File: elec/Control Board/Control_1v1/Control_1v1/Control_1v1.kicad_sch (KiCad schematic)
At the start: 163 parts, among them J1 DB9_Female_MountingHoles, J10 Conn_02x12_Odd_Even, J11 Screw_Terminal_01x02, J14 Conn_01x10, J2 Conn_01x08, J25 Screw_Terminal_01x02, J26 Conn_01x10, J27 Conn_02x12_Odd_Even, J28 Screw_Terminal_01x02, J29 Conn_01x10, J3 Conn_01x08, J37 Conn_01x04, J4 Conn_01x08, J5 Conn_01x08, J6 Conn_01x08, J7 Conn_01x10, J8 Conn_02x18_Odd_Even, J9 Conn_01x10, Q601 BSS138

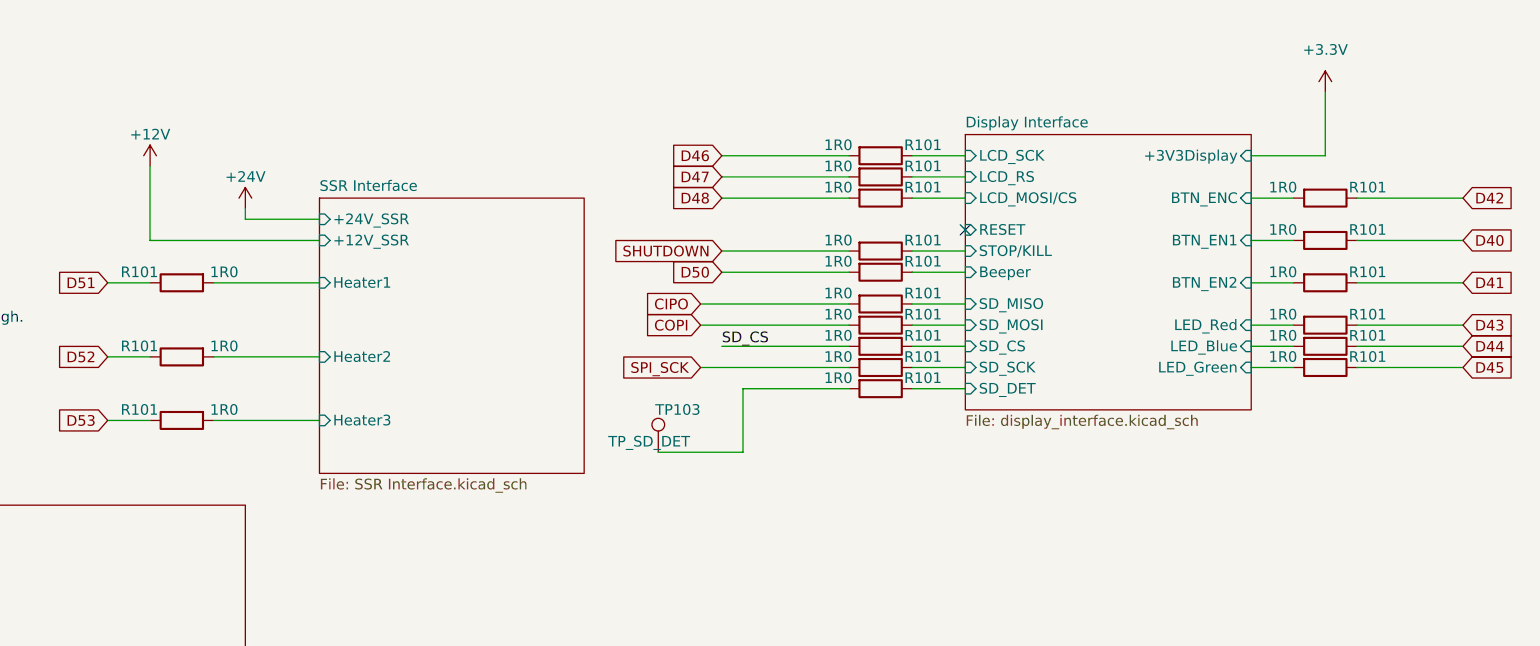
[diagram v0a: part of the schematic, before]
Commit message: Update schematic to reflect some reworks to V1.1 assemblies. 5V to Display. Display signal names. J35 pin8 to 10 short.
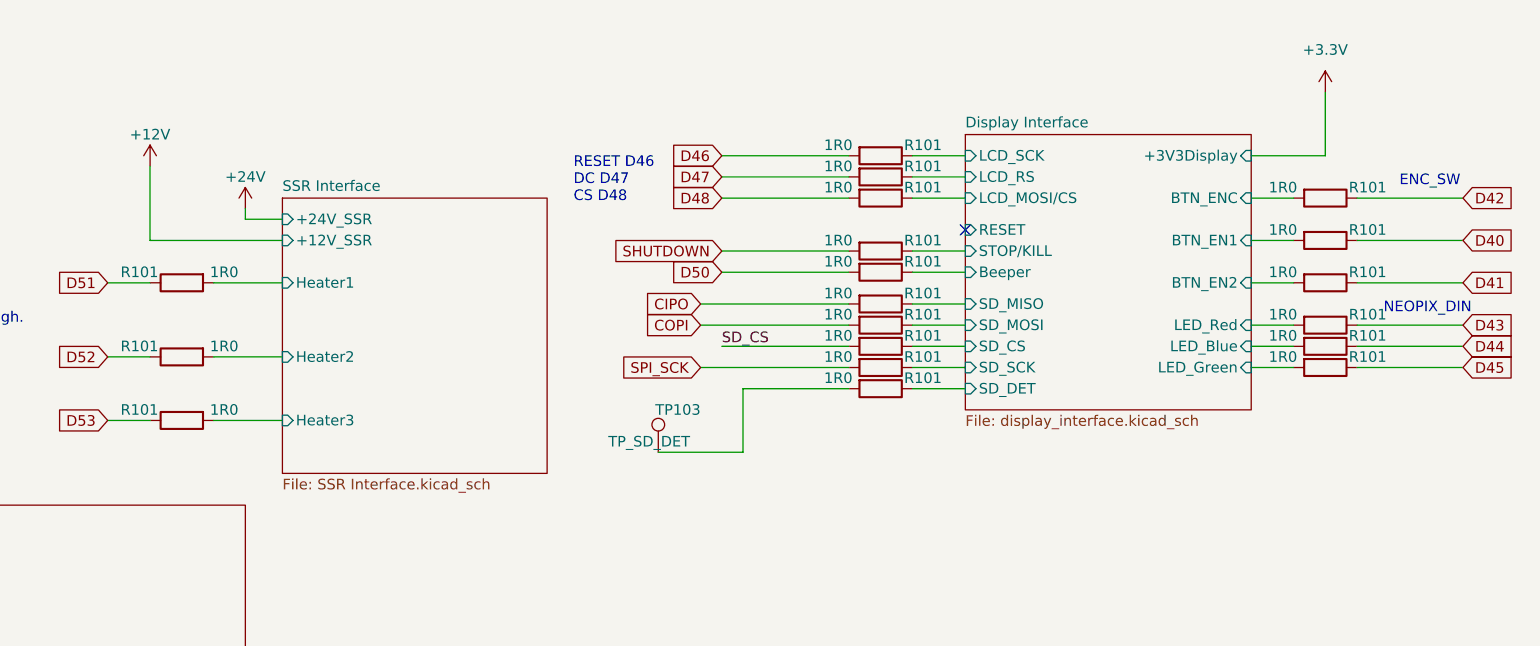
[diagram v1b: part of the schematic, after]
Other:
- note added: "ENC_SW"
- note added: "NEOPIX_DIN"
- note added: "RESET D46 DC D47 CS D48"
- title: Control Interconnect Board OEDCS -> Control Interconnect Board OEDCS With Reworks
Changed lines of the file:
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@@
   (paper "User" 533.4 330.2)
   (title_block
-    (title "Control Interconnect Board OEDCS")
-    (date "2023-10-10")
+    (title "Control Interconnect Board OEDCS With Reworks")
+    (date "2023-12-06")
     (rev "Rev 1.1")
     (company "Public Invention")
@@
     (stroke (width 0) (type default))
   )
-  (wire (pts (xy 377.19 248.92) (xy 368.3 248.92))
+  (wire (pts (xy 372.745 248.92) (xy 368.3 248.92))
     (stroke (width 0) (type default))
   )
@@
     (stroke (width 0) (type default))
   )
-  (wire (pts (xy 364.49 265.43) (xy 377.19 265.43))
+  (wire (pts (xy 364.49 265.43) (xy 372.745 265.43))
     (stroke (width 0) (type default))
   )
@@
     (stroke (width 0) (type default))
   )
-  (wire (pts (xy 364.49 256.54) (xy 377.19 256.54))
+  (wire (pts (xy 364.49 256.54) (xy 372.745 256.54))
     (stroke (width 0) (type default))
   )
@@
     (stroke (width 0) (type default))
   )
-  (wire (pts (xy 364.49 273.05) (xy 377.19 273.05))
+  (wire (pts (xy 364.49 273.05) (xy 372.745 273.05))
     (stroke (width 0) (type default))
   )
@@
     (stroke (width 0) (type default))
   )
-  (wire (pts (xy 377.19 251.46) (xy 356.87 251.46))
+  (wire (pts (xy 372.745 251.46) (xy 356.87 251.46))
     (stroke (width 0) (type default))
   )
@@
     (effects (font (size 1.27 1.27)) (justify left bottom))
   )
+  (text "ENC_SW" (at 506.73 245.11 0)
+    (effects (font (size 1.27 1.27)) (justify left bottom))
+  )
   (text "Blower Controller Signals\nFAN_POWER the Due output sets high to enable power to the blower.\nFAN1_FG is the Due input gets tachometer signal. Two low going edeges per revoluion.\nnFan1_PWM is negative aserted PWM to control blower speed."
     (at 302.26 189.23 0)
     (effects (font (size 1.27 1.27)) (justify left bottom))
   )
+  (text "NEOPIX_DIN" (at 504.825 260.35 0)
+    (effects (font (size 1.27 1.27)) (justify left bottom))
+  )
   (text "Logic Level i2c Connector" (at 35.56 287.02 0)
     (effects (font (size 1.27 1.27)) (justify left bottom))
@@
     (effects (font (size 1.27 1.27)) (justify left bottom))
   )
+  (text "RESET D46\nDC D47\nCS D48" (at 407.67 247.015 0)
+    (effects (font (size 1.27 1.27)) (justify left bottom))
+  )
   (text "One Wire Thermocouple amplifiter and Interface\nDATA is bidorectional on the Due GPIO"
     (at 92.71 154.94 0)
@@
     )
   )
-  (sheet (at 377.19 246.38) (size 31.75 33.02) (fields_autoplaced)
+  (sheet (at 372.745 246.38) (size 31.75 33.02) (fields_autoplaced)
     (stroke (width 0.1524) (type solid))
     (fill (color 0 0 0 0.0000))
-    (property "Sheetname" "SSR Interface" (at 377.19 245.6684 0)
+    (property "Sheetname" "SSR Interface" (at 372.745 245.6684 0)
       (effects (font (size 1.27 1.27)) (justify left bottom))
     )
-    (property "Sheetfile" "SSR Interface.kicad_sch" (at 377.19 279.9846 0)
+    (property "Sheetfile" "SSR Interface.kicad_sch" (at 372.745 279.9846 0)
       (effects (font (size 1.27 1.27)) (justify left top))
     )
-    (pin "+24V_SSR" input (at 377.19 248.92 180)
+    (pin "+24V_SSR" input (at 372.745 248.92 180)
       (effects (font (size 1.27 1.27)) (justify left))
     )
-    (pin "+12V_SSR" input (at 377.19 251.46 180)
+    (pin "+12V_SSR" input (at 372.745 251.46 180)
       (effects (font (size 1.27 1.27)) (justify left))
     )
-    (pin "Heater1" input (at 377.19 256.54 180)
+    (pin "Heater1" input (at 372.745 256.54 180)
       (effects (font (size 1.27 1.27)) (justify left))
     )
-    (pin "Heater2" input (at 377.19 265.43 180)
+    (pin "Heater2" input (at 372.745 265.43 180)
       (effects (font (size 1.27 1.27)) (justify left))
     )
-    (pin "Heater3" input (at 377.19 273.05 180)
+    (pin "Heater3" input (at 372.745 273.05 180)
       (effects (font (size 1.27 1.27)) (justify left))
     )

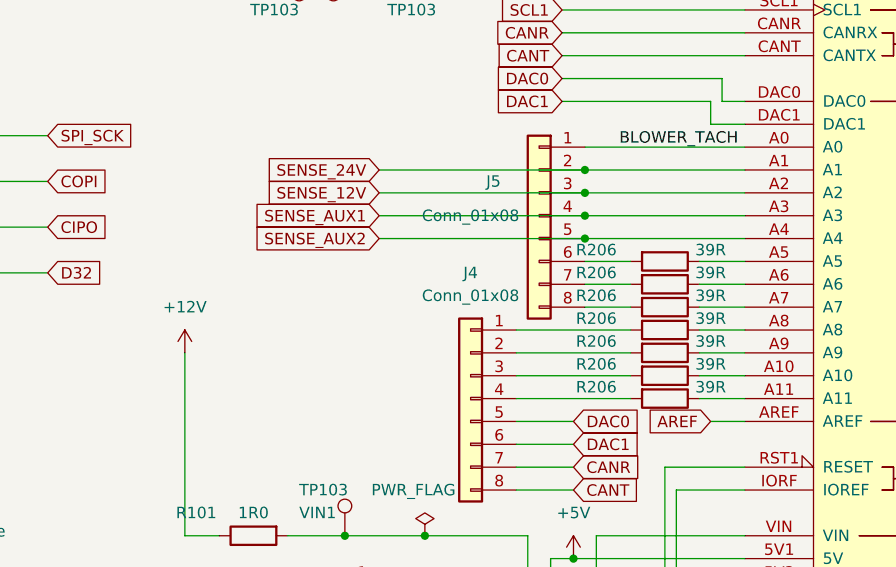
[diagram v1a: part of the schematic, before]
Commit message: Add R1 and R2 arguments to ADC Class. Show Rework for SENSE_AUX2 on schematic.
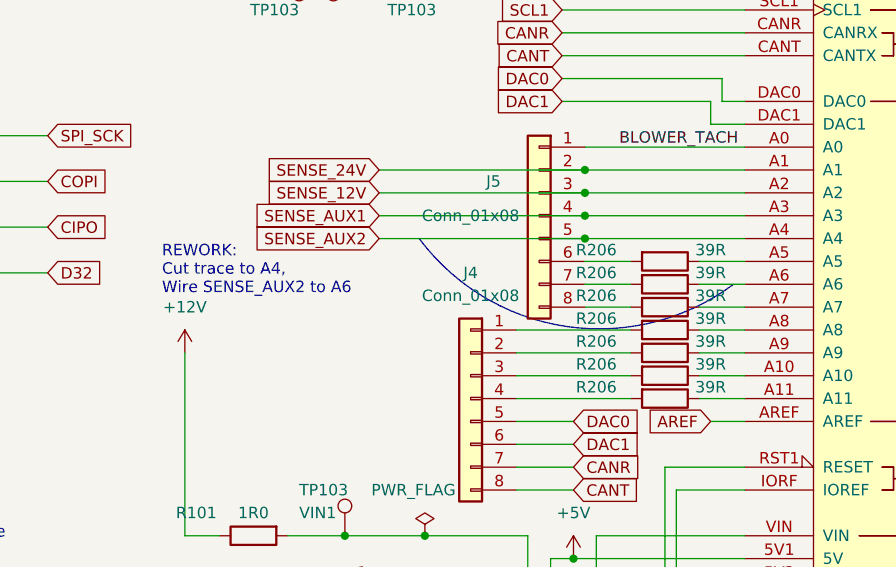
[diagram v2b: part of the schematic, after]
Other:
- note added: "REWORK: Cut trace to A4, Wire SENSE_AUX2 to A6"
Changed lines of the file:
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@@
     (stroke (width 0) (type default))
+  )
+  (arc (start 215.9 124.46) (mid 197.3854 129.1532) (end 180.975 119.38)
+    (stroke (width 0) (type default))
+    (fill (type none))
   )
   (image (at 508 294.64) (scale 0.75)
@@
     (effects (font (size 1.27 1.27)) (justify left bottom))
   )
+  (text "REWORK:\nCut trace to A4,\nWire SENSE_AUX2 to A6" (at 152.4 125.73 0)
+    (effects (font (size 1.27 1.27)) (justify left bottom))
+  )

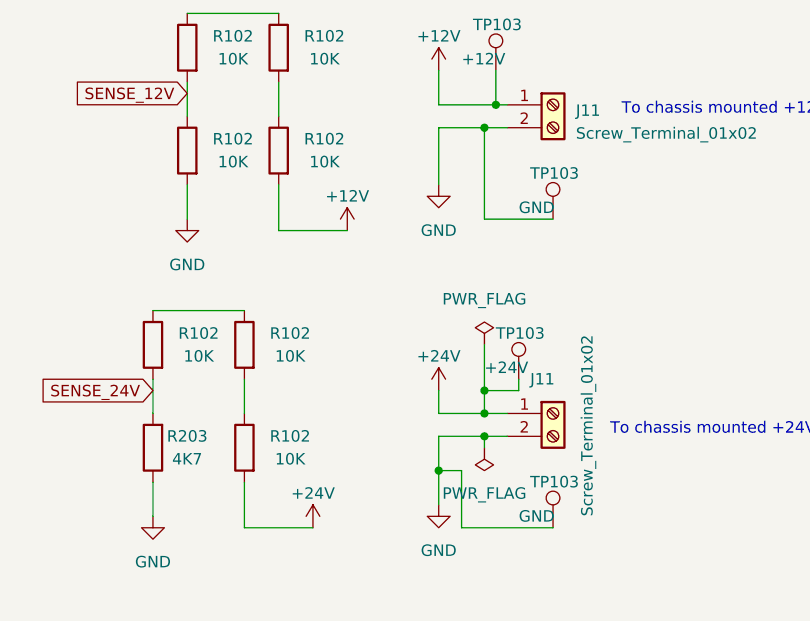
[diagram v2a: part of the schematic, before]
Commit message: Add notes about reworkd to R106 and R108.
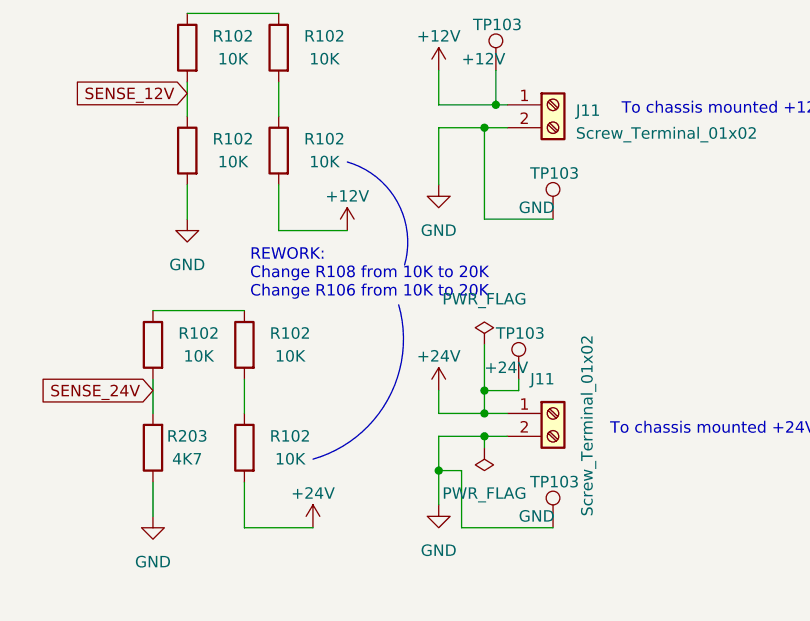
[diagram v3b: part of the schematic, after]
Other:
- note added: "REWORK: Change R108 from 10K to 20K Change R106 from 10K to 20K"
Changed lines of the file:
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@@
     (stroke (width 0) (type default))
   )
+  (arc (start 448.31 175.26) (mid 453.8576 179.6643) (end 454.678 186.7)
+    (stroke (width 0) (type default))
+    (fill (type none))
+  )
   (arc (start 215.9 124.46) (mid 197.3854 129.1532) (end 180.975 119.38)
+    (stroke (width 0) (type default))
+    (fill (type none))
+  )
+  (arc (start 454.025 191.135) (mid 452.8081 201.6773) (end 444.5 208.28)
     (stroke (width 0) (type default))
     (fill (type none))
@@
     (effects (font (size 1.27 1.27)) (justify left bottom))
   )
+  (text "REWORK:\nChange R108 from 10K to 20K\nChange R106 from 10K to 20K"
+    (at 437.515 190.5 0)
+    (effects (font (size 1.27 1.27)) (justify left bottom))
+  )

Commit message: Add notes to schematic about level shifting 5V to 3.3V on Stack Power Supply. More annotation of many schematic blocks.
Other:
- note added: "5V PS to 3.3V Due REWORK: Change R14 from 1R0 to 1K, Add a 2K to GND. Change R100 from 1R0 to 1K, Add a 2K to GND."
- note added: "Breadboarding Area Patterned off of solderless breadboard"
- note added: "Connectors to Stack Power Supplies"
- note added: "Investiage: Are level shifters required on I2C from Power supplies to Due? --->"
- note added: "MAX31850"
- note added: "MAX31855"
- note added: "MCP9600"
- note added: "Mouting Holes"
- note added: "One Wire Thermocouple amplifiter DATA is bidirectional GPIO"
- note added: "Power Input, 12V and 24V."
- note added: "SPI on RJ12"
- note added: "SSR Interface (Solid State Relay) Provide +24 to SSR (or +12 with resistor change) D51, D52 and D53 are asserted high to close relay."
- note added: "Thermocouple amplifiter DATA is I2C"
- note added: "Thermocouple amplifiter DATA is SPI"
- note removed: "One Wire Thermocouple amplifiter and Interface DATA is bidorectional on the Due GPIO"
- note removed: "SSR Interface (Solid State Relay) HEATER the Due output sets high to switch AC power to enable preheaters Heater_SSR_High passes +5V through to the SSR. Heater_SSR_High goes low, conducts, to turn on SSR when HEATER is asserted high."
- moved on the sheet: C301, J1, J11, J37, R101, R102, R203, TP103
